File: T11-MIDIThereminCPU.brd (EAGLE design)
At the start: 76.2 x 61 mm, 55 parts, among them IC1 UA78M05DCY, IC5 4069D, J1 DCJ0202, Q1 16MHz, U1 ATMEGA328P-AU

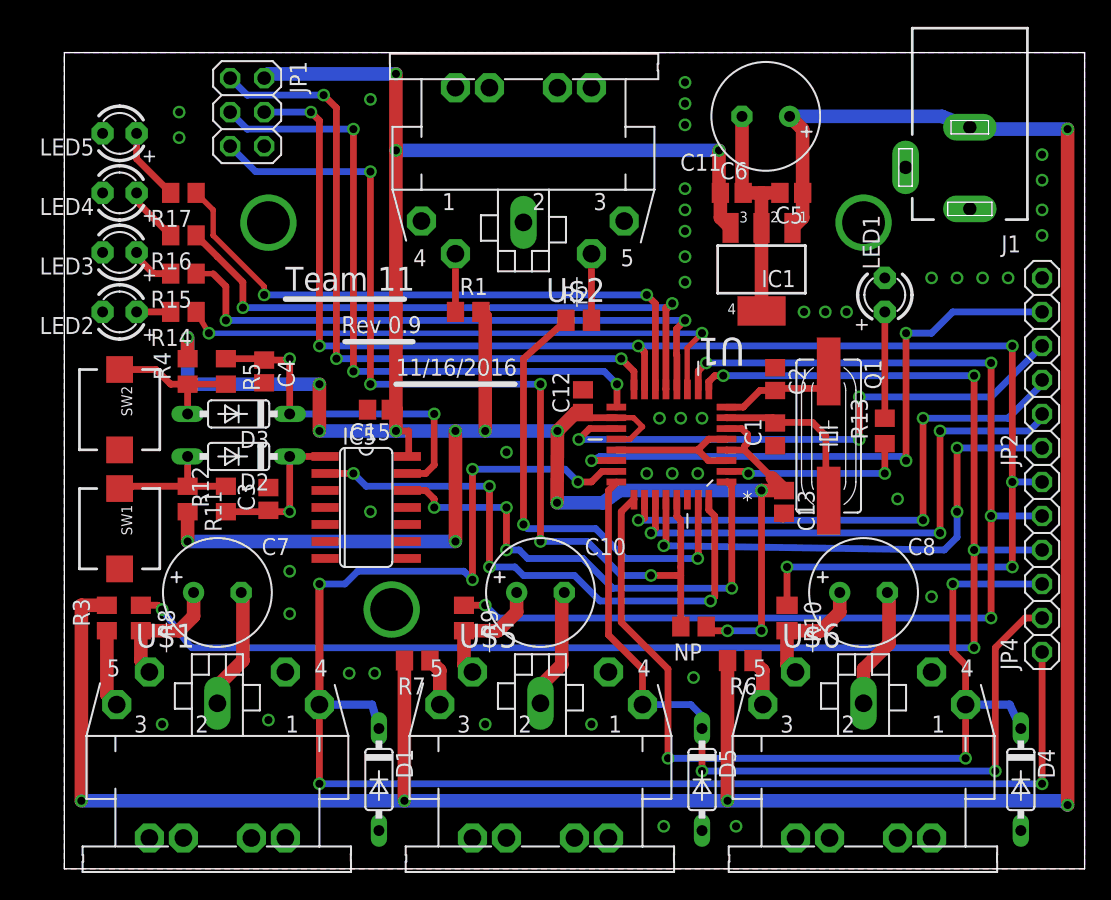
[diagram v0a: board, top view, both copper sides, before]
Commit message: added a jumper to the MOSI line for programming
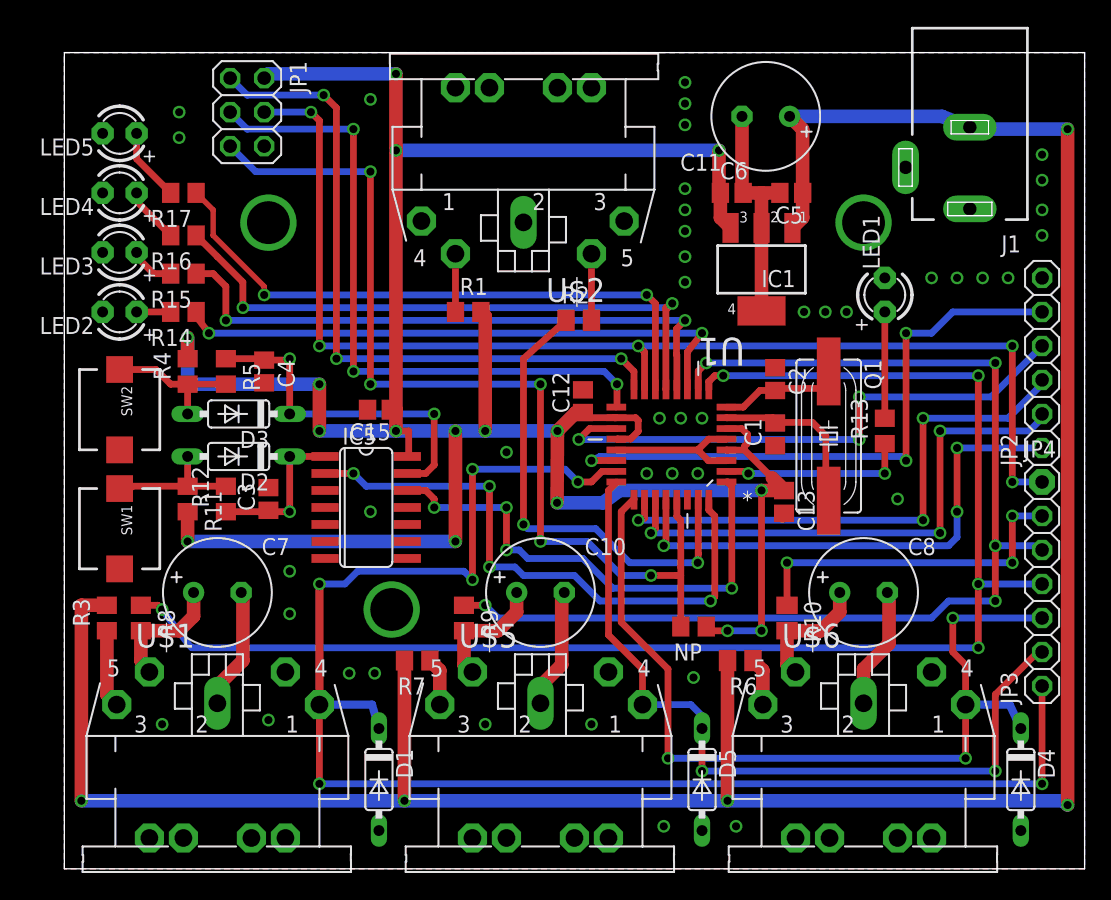
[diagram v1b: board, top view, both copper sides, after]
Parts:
- added JP3: (no value), adafruit:1X06
- D2, D3: value 0.7v Drop -> 1N4148DO35-7
- JP4: device adafruit:1X06 -> adafruit:1X01
- moved JP4 6.35 mm to (73.0, 28.9), turned to 0 degrees
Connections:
- new net MOSI_PWM: JP3.6, R10.1
- net ANALOG_IN_1: now also JP3.1; no longer JP4.1
- net ANALOG_IN_2: now also JP3.2; no longer JP4.2
- net ANALOG_IN_3: now also JP3.3; no longer JP4.3
- net MOSI: now also JP4.1; no longer JP4.6, R10.1
- net SIGNAL_OUT_1: now also JP3.4; no longer JP4.4
- net SIGNAL_OUT_2: now also JP3.5; no longer JP4.5
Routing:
- net MOSI: track 114.8 -> 88.8 mm, vias 7 -> 5
- net MOSI_PWM: track 0.00 -> 25.7 mm, vias 0 -> 3
- net ANALOG_IN_2: track 62.4 -> 59.7 mm
- net ANALOG_IN_1: track 116.3 -> 113.8 mm
- net ANALOG_IN_3: track 68.8 -> 66.3 mm
- net GND: vias 46 -> 45
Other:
- board text removed: "11/16/2016"
- board text removed: "Rev 0.9"
- board text removed: "Team 11"

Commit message: removed debounce circuit. added vias
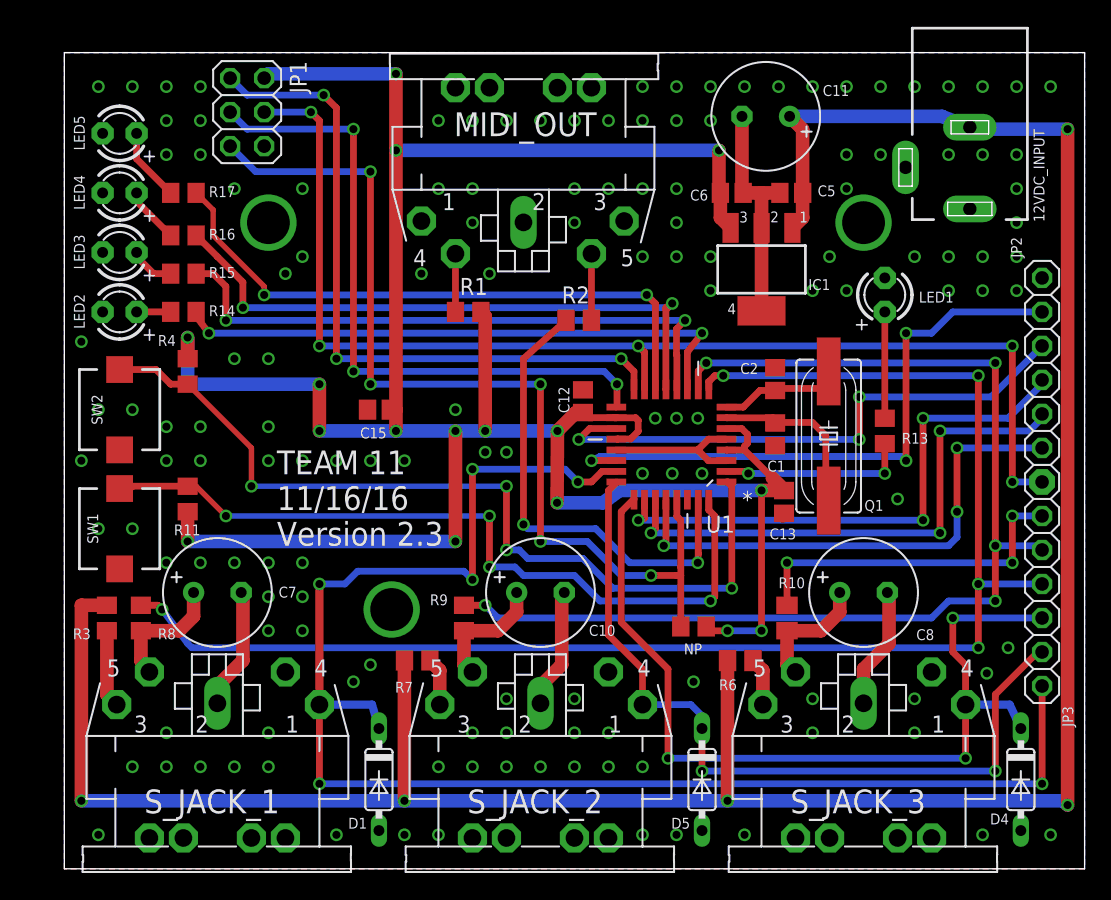
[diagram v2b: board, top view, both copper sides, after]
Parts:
- removed C3, C4: 1u, adafruit:C0805
- removed D2, D3: 1N4148DO35-7, diode:DO35-7
- removed IC5: 4069D, 40xx:SO14
- removed R12, R5: 18k, resistor:R0805
- R11, R4: value 82k -> 10k
- renumbered J1 to 12VDC_INPUT, U$1 to S_JACK_1, U$2 to MIDI_OUT, U$5 to S_JACK_2, U$6 to S_JACK_3
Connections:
- removed net N$11: D2.A, R11.1, R12.2, SW1.P$2
- removed net N$14: C3.1, D2.C, IC5.1, R12.1
- removed net N$4: D3.A, R4.1, R5.2, SW2.P$2
- removed net N$6: C4.1, D3.C, IC5.13, R5.1
- net +5V: no longer IC5.14
- net GND: no longer C3.2, C4.2, IC5.11, IC5.3, IC5.5, IC5.7, IC5.9
- net INT0: now also R11.1, SW1.P$2; no longer IC5.2
- net INT1: now also R4.1, SW2.P$2; no longer IC5.12
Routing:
- net INT1: track 37.6 -> 65.1 mm
- net N$6: track 25.8 -> 0.00 mm, vias 2 -> 0
- net ADC7: track 45.9 -> 68.4 mm
- net INT0: track 44.2 -> 57.9 mm
- net N$14: track 11.8 -> 0.00 mm, vias 1 -> 0
- net N$4: track 10.6 -> 0.00 mm
- net N$11: track 10.2 -> 0.00 mm
- net +5V: track 202.9 -> 200.0 mm
- net GND: track 56.4 -> 56.2 mm, vias 45 -> 145
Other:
- board text added: "TEAM 11 11/16/16 Version 2.3"

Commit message: added optional panel mount buttons
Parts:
- added JP5, JP6, JP7, JP8: (no value), pinhead:1X01
- JP4: device adafruit:1X01 -> pinhead:1X01
- moved SW1 0.64 mm to (3.49, 25.4)
- moved SW2 0.64 mm to (3.49, 34.3)
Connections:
- net GND: now also JP6.1, JP8.1
- net INT0: now also JP5.1
- net INT1: now also JP7.1
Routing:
- net INT1: track 65.1 -> 68.8 mm
- net INT0: track 57.9 -> 60.6 mm
- net GND: vias 145 -> 136
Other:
- board text added: "TEAM 11 11/16/16 Version 2.4"
- board text removed: "TEAM 11 11/16/16 Version 2.3"
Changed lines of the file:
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@@
 <setting verticaltext="up"/>
 </settings>
-<grid distance="0.1" unitdist="inch" unit="inch" style="lines" multiple="1" display="yes" altdistance="0.025" altunitdist="inch" altunit="inch"/>
+<grid distance="0.0125" unitdist="inch" unit="inch" style="lines" multiple="1" display="yes" altdistance="0.025" altunitdist="inch" altunit="inch"/>
 <layers>
 <layer number="1" name="Top" color="4" fill="1" visible="yes" active="yes"/>
@@
 <wire x1="76.2" y1="60.96" x2="0" y2="60.96" width="0" layer="20"/>
 <wire x1="0" y1="60.96" x2="0" y2="0" width="0" layer="20"/>
-<text x="15.875" y="24.13" size="1.778" layer="25">TEAM 11
+<text x="16.51" y="22.225" size="1.778" layer="25">TEAM 11
 11/16/16
-Version 2.3</text>
+Version 2.4</text>
 </plain>
 <attributes>
@@
 <attribute name="VALUE" x="27.305" y="19.3675" size="1.27" layer="27" rot="R270"/>
 </element>
-<element name="SW1" library="adafruit" package="PUSHBUTTON_SMD_SJ" value="" x="4.1275" y="25.4" smashed="yes" rot="R270">
-<attribute name="NAME" x="1.7145" y="26.543" size="0.8128" layer="25" ratio="18" rot="R270"/>
-<attribute name="VALUE" x="3.3655" y="27.178" size="0.4064" layer="27" ratio="10" rot="R270"/>
-</element>
-<element name="SW2" library="adafruit" package="PUSHBUTTON_SMD_SJ" value="" x="4.1275" y="34.29" smashed="yes" rot="R270">
-<attribute name="NAME" x="2.032" y="35.433" size="0.8128" layer="25" ratio="18" rot="R270"/>
-<attribute name="VALUE" x="3.3655" y="36.068" size="0.4064" layer="27" ratio="10" rot="R270"/>
+<element name="SW1" library="adafruit" package="PUSHBUTTON_SMD_SJ" value="" x="3.4925" y="25.4" smashed="yes" rot="R270">
+<attribute name="NAME" x="1.0795" y="26.543" size="0.8128" layer="25" ratio="18" rot="R270"/>
+<attribute name="VALUE" x="2.7305" y="27.178" size="0.4064" layer="27" ratio="10" rot="R270"/>
+</element>
+<element name="SW2" library="adafruit" package="PUSHBUTTON_SMD_SJ" value="" x="3.4925" y="34.29" smashed="yes" rot="R270">
+<attribute name="NAME" x="1.397" y="35.433" size="0.8128" layer="25" ratio="18" rot="R270"/>
+<attribute name="VALUE" x="2.7305" y="36.068" size="0.4064" layer="27" ratio="10" rot="R270"/>
 </element>
 <element name="S_JACK_1" library="adafruit" package="CP-2350" value="MIDIJACK" x="11.43" y="-0.3175" smashed="yes">
@@
 <attribute name="VALUE" x="76.2" y="30.1625" size="1.27" layer="27" rot="R90"/>
 </element>
-<element name="JP4" library="adafruit" package="1X01" value="" x="73.025" y="28.8925" smashed="yes">
+<element name="JP4" library="pinhead" package="1X01" value="" x="73.025" y="28.8925" smashed="yes">
 <attribute name="VALUE" x="71.755" y="25.7175" size="1.27" layer="27"/>
 </element>
@@
 <attribute name="NAME" x="74.5363" y="12.1412" size="0.8128" layer="25" ratio="10" rot="R270"/>
 <attribute name="VALUE" x="76.2" y="12.3825" size="1.27" layer="27" rot="R90"/>
+</element>
+<element name="JP5" library="pinhead" package="1X01" value="" x="6.35" y="28.575" smashed="yes">
+<attribute name="VALUE" x="5.08" y="25.4" size="1.27" layer="27"/>
+</element>
+<element name="JP6" library="pinhead" package="1X01" value="" x="3.4925" y="34.29" smashed="yes">
+<attribute name="VALUE" x="2.2225" y="31.115" size="1.27" layer="27"/>
+</element>
+<element name="JP7" library="pinhead" package="1X01" value="" x="6.35" y="37.465" smashed="yes">
+<attribute name="VALUE" x="5.08" y="34.29" size="1.27" layer="27"/>
+</element>
+<element name="JP8" library="pinhead" package="1X01" value="" x="3.4925" y="25.4" smashed="yes">
+<attribute name="VALUE" x="2.2225" y="22.225" size="1.27" layer="27"/>
 </element>
 </elements>
@@
 <via x="44.1325" y="33.655" extent="1-16" drill="0.6"/>
 <via x="31.4325" y="31.115" extent="1-16" drill="0.6"/>
-<via x="17.78" y="22.86" extent="1-16" drill="0.6"/>
-<via x="7.62" y="22.86" extent="1-16" drill="0.6"/>
-<via x="5.08" y="25.4" extent="1-16" drill="0.6"/>
-<via x="2.54" y="25.4" extent="1-16" drill="0.6"/>
 <via x="46.99" y="13.97" extent="1-16" drill="0.6"/>
 <via x="22.86" y="15.24" extent="1-16" drill="0.6"/>
@@
 <via x="29.21" y="34.29" extent="1-16" drill="0.6"/>
 <via x="57.15" y="45.72" extent="1-16" drill="0.6"/>
-<via x="2.54" y="34.29" extent="1-16" drill="0.6"/>
-<via x="5.08" y="34.29" extent="1-16" drill="0.6"/>
-<via x="1.27" y="30.48" extent="1-16" drill="0.6"/>
 <via x="1.27" y="39.37" extent="1-16" drill="0.6"/>
 <via x="16.51" y="44.45" extent="1-16" drill="0.6"/>
@@
 <via x="10.16" y="30.48" extent="1-16" drill="0.6"/>
 <via x="10.16" y="33.02" extent="1-16" drill="0.6"/>
-<via x="7.62" y="33.02" extent="1-16" drill="0.6"/>
-<via x="7.62" y="30.48" extent="1-16" drill="0.6"/>
 <via x="15.24" y="38.1" extent="1-16" drill="0.6"/>
 <via x="12.7" y="38.1" extent="1-16" drill="0.6"/>
@@
 <via x="40.64" y="50.8" extent="1-16" drill="0.6"/>
 <via x="43.18" y="50.8" extent="1-16" drill="0.6"/>
+<contactref element="JP8" pad="1"/>
+<contactref element="JP6" pad="1"/>
 </signal>
 <signal name="MISO">
@@
 <contactref element="SW1" pad="P$2"/>
 <wire x1="9.205" y1="28.575" x2="9.2075" y2="28.5725" width="0.508" layer="1"/>
-<wire x1="9.205" y1="28.575" x2="5.08" y2="28.575" width="0.508" layer="1"/>
+<wire x1="9.205" y1="28.575" x2="6.35" y2="28.575" width="0.508" layer="1"/>
+<wire x1="6.35" y1="28.575" x2="5.08" y2="28.575" width="0.508" layer="1"/>
 <wire x1="5.08" y1="28.575" x2="4.905" y2="28.4" width="0.508" layer="1"/>
-<wire x1="4.905" y1="28.4" x2="4.1275" y2="28.4" width="0.508" layer="1"/>
+<wire x1="4.905" y1="28.4" x2="4.445" y2="28.4" width="0.508" layer="1"/>
+<wire x1="4.445" y1="28.4" x2="3.4925" y2="28.4" width="0.508" layer="1"/>
 <wire x1="31.75" y1="26.3525" x2="12.065" y2="26.3525" width="0.4064" layer="16"/>
 <via x="12.065" y="26.3525" extent="1-16" drill="0.6"/>
@@
 <wire x1="9.8425" y1="28.575" x2="9.21" y2="28.575" width="0.4064" layer="1"/>
 <wire x1="9.21" y1="28.575" x2="9.2075" y2="28.5725" width="0.4064" layer="1"/>
+<contactref element="JP5" pad="1"/>
+<wire x1="6.35" y1="28.575" x2="4.445" y2="28.575" width="0.4064" layer="1"/>
+<wire x1="4.445" y1="28.575" x2="4.445" y2="28.4" width="0.4064" layer="1"/>
 </signal>
 <signal name="N$2">
@@
 <contactref element="SW2" pad="P$2"/>
 <contactref element="R4" pad="1"/>
-<wire x1="4.1275" y1="37.29" x2="6.8425" y2="37.29" width="0.508" layer="1"/>
+<wire x1="3.4925" y1="37.29" x2="6.8425" y2="37.29" width="0.508" layer="1"/>
 <wire x1="6.8425" y1="37.29" x2="7.9375" y2="36.195" width="0.508" layer="1"/>
 <wire x1="7.9375" y1="36.195" x2="9.205" y2="36.195" width="0.508" layer="1"/>
@@
 <wire x1="13.97" y1="28.575" x2="13.97" y2="31.435" width="0.4064" layer="1"/>
 <wire x1="13.97" y1="31.435" x2="9.2075" y2="36.1975" width="0.4064" layer="1"/>
+<contactref element="JP7" pad="1"/>
+<wire x1="6.35" y1="37.465" x2="3.4925" y2="37.465" width="0.4064" layer="1"/>
+<wire x1="3.4925" y1="37.465" x2="3.4925" y2="37.29" width="0.4064" layer="1"/>
 </signal>
 <signal name="N$5">
